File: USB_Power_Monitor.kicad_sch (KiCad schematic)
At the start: 55 parts, among them IC1 MCS1826GQTE-05-P, J1 USB_C_Receptacle, J2 USB_C_Plug, J5 Conn_01x01, J6 Conn_01x01, SW1 SW_Push_Dual, U1 RP2040, U2 L7983PU33R, U3 W25Q16JVSS, U4 TS3USB221AQRSERQ1, Y1 ABM8-272-T3

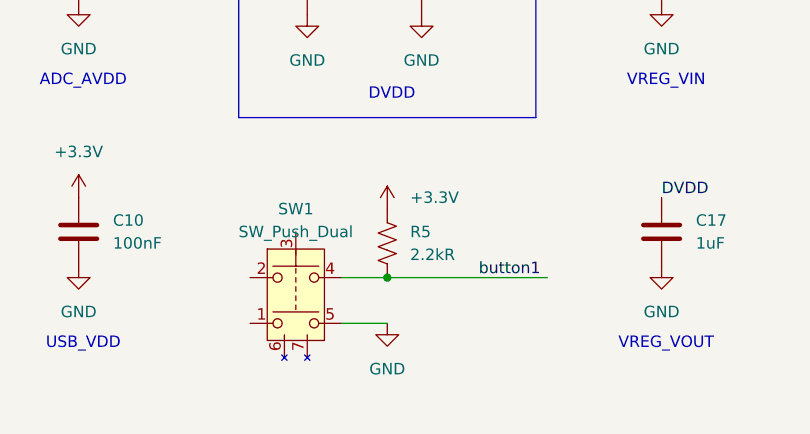
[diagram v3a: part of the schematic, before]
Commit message: All nets routed, need to clean up text and check errors
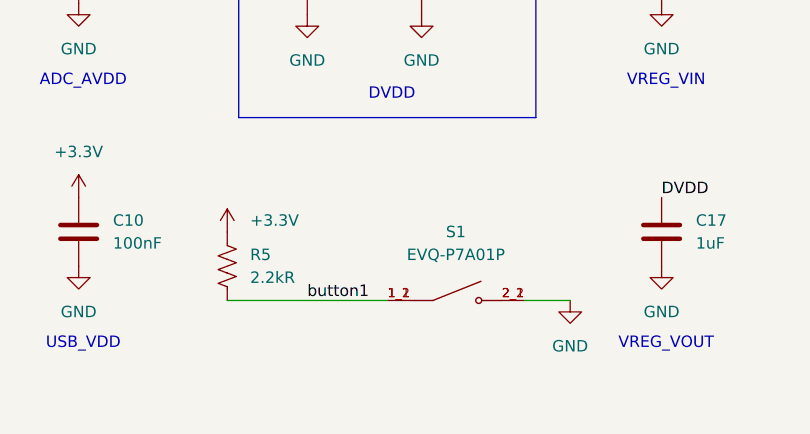
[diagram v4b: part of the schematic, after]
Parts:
- removed SW1: SW_Push_Dual, KMS231GPLFS:SMT_231GPLFS, symbol Switch:SW_Push_Dual
- added S1: EVQ-P7A01P, EVQ-P7A01P:SW_EVQ-P7A01P, symbol EVQ-P7A01P:EVQ-P7A01P
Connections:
- net GND: now also S1.2_1, S1.2_2
- net button1: now also S1.1_1, S1.1_2
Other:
- moved on the sheet: R5
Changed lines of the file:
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@@
 	)
 	(junction
-		(at 59.69 180.34)
-		(diameter 0)
-		(color 0 0 0 0)
-	)
-	(junction
 		(at 224.79 114.3)
 		(diameter 0)
@@
 	(wire
 		(pts
-			(xy 59.69 180.34) (xy 77.47 180.34)
+			(xy 41.91 182.88) (xy 59.69 182.88)
 		)
 		(stroke
@@
 	(wire
 		(pts
-			(xy 54.61 180.34) (xy 59.69 180.34)
-		)
-		(stroke
-			(width 0)
-			(type default)
-		)
-	)
-	(wire
-		(pts
 			(xy 138.43 59.69) (xy 149.86 59.69)
 		)
@@
 	(wire
 		(pts
-			(xy 54.61 185.42) (xy 59.69 185.42)
+			(xy 74.93 182.88) (xy 80.01 182.88)
 		)
 		(stroke
@@
 	)
 	(label "button1"
-		(at 69.85 180.34 0)
+		(at 50.8 182.88 0)
 		(effects
 			(font
@@
 	(symbol
 		(lib_id "power:+3.3V")
-		(at 59.69 172.72 0)
+		(at 41.91 175.26 0)
 		(unit 1)
 		(exclude_from_sim no)
@@
 		(fields_autoplaced yes)
 		(property "Reference" "#PWR052"
-			(at 59.69 176.53 0)
+			(at 41.91 179.07 0)
 			(effects
 				(font
@@
 		)
 		(property "Value" "+3.3V"
-			(at 62.23 171.4499 0)
+			(at 44.45 173.9899 0)
 			(effects
 				(font
@@
 		)
 		(property "Footprint" ""
-			(at 59.69 172.72 0)
+			(at 41.91 175.26 0)
 			(effects
 				(font
@@
 		)
 		(property "Datasheet" ""
-			(at 59.69 172.72 0)
+			(at 41.91 175.26 0)
 			(effects
 				(font
@@
 		)
 		(property "Description" "Power symbol creates a global label with name \"+3.3V\""
-			(at 59.69 172.72 0)
+			(at 41.91 175.26 0)
 			(effects
 				(font
@@
 	)
 	(symbol
-		(lib_id "Switch:SW_Push_Dual")
-		(at 49.53 182.88 0)
-		(unit 1)
-		(exclude_from_sim no)
-		(in_bom yes)
-		(on_board yes)
-		(dnp no)
-		(fields_autoplaced yes)
-		(property "Reference" "SW1"
-			(at 49.53 172.72 0)
-			(effects
-				(font
-					(size 1.27 1.27)
-				)
-			)
-		)
-		(property "Value" "SW_Push_Dual"
-			(at 49.53 175.26 0)
-			(effects
-				(font
-					(size 1.27 1.27)
-				)
-			)
-		)
-		(property "Footprint" "KMS231GPLFS:SMT_231GPLFS"
-			(at 49.53 175.26 0)
-			(effects
-				(font
-					(size 1.27 1.27)
-				)
-				(hide yes)
-			)
-		)
-		(property "Datasheet" "~"
-			(at 49.53 182.88 0)
-			(effects
-				(font
-					(size 1.27 1.27)
-				)
-				(hide yes)
-			)
-		)
-		(property "Description" "Push button switch, generic, symbol, four pins"
-			(at 49.53 182.88 0)
-			(effects
-				(font
-					(size 1.27 1.27)
-				)
-				(hide yes)
-			)
-		)
-		(property "KLC_S4.2_DVDD" ""
-			(at 49.53 182.88 0)
-			(effects
-				(font
-					(size 1.27 1.27)
-				)
-				(hide yes)
-			)
-		)
-		(property "KLC_S4.2_VREG_VOUT" ""
-			(at 49.53 182.88 0)
-			(effects
-				(font
-					(size 1.27 1.27)
-				)
-				(hide yes)
-			)
-		)
-		(property "Manufacturer_Name" "C&K"
-			(at 49.53 182.88 0)
-			(effects
-				(font
-					(size 1.27 1.27)
-				)
-				(hide yes)
-			)
-		)
-		(property "Manufacturer_Part_Number" "KMS231GP LFS"
-			(at 49.53 182.88 0)
-			(effects
-				(font
-					(size 1.27 1.27)
-				)
-				(hide yes)
-			)
-		)
-		(pin "4"
-		)
-		(pin "2"
-		)
-		(pin "3"
-		)
-		(pin "1"
-		)
-		(pin "5"
-		)
-		(pin "7"
-		)
-		(pin "6"
-		)
-		(instances
-			(project ""
-				(path "/e9e64cba-d7b8-4c36-9924-3031f0f5d4f4"
-					(reference "SW1")
-					(unit 1)
-				)
-			)
-		)
-	)
-	(symbol
 		(lib_id "power:GND")
 		(at 73.66 87.63 0)
@@
 	)
 	(symbol
+		(lib_id "EVQ-P7A01P:EVQ-P7A01P")
+		(at 67.31 182.88 0)
+		(unit 1)
+		(exclude_from_sim no)
+		(in_bom yes)
+		(on_board yes)
+		(dnp no)
+		(fields_autoplaced yes)
+		(property "Reference" "S1"
+			(at 67.31 175.26 0)
+			(effects
+				(font
+					(size 1.27 1.27)
+				)
+			)
+		)
+		(property "Value" "EVQ-P7A01P"
+			(at 67.31 177.8 0)
+			(effects
+				(font
+					(size 1.27 1.27)
+				)
+			)
+		)
+		(property "Footprint" "EVQ-P7A01P:SW_EVQ-P7A01P"
+			(at 67.31 182.88 0)
+			(effects
+				(font
+					(size 1.27 1.27)
+				)
+				(justify bottom)
+				(hide yes)
+			)
+		)
+		(property "Datasheet" ""
+			(at 67.31 182.88 0)
+			(effects
+				(font
+					(size 1.27 1.27)
+				)
+				(hide yes)
+			)
+		)
+		(property "Description" ""
+			(at 67.31 182.88 0)
+			(effects
+				(font
+					(size 1.27 1.27)
+				)
+				(hide yes)
+			)
+		)
+		(property "PARTREV" "2022.4"
+			(at 67.31 182.88 0)
+			(effects
+				(font
+					(size 1.27 1.27)
+				)
+				(justify bottom)
+				(hide yes)
+			)
+		)
+		(property "STANDARD" "Manufacturer Recommendations"
+			(at 67.31 182.88 0)
+			(effects
+				(font
+					(size 1.27 1.27)
+				)
+				(justify bottom)
+				(hide yes)
+			)
+		)
+		(property "MAXIMUM_PACKAGE_HEIGHT" "1.35mm"
+			(at 67.31 182.88 0)
+			(effects
+				(font
+					(size 1.27 1.27)
+				)
+				(justify bottom)
+				(hide yes)
+			)
+		)
+		(property "MANUFACTURER" "Panasonic Electronic Components"
+			(at 67.31 182.88 0)
+			(effects
+				(font
+					(size 1.27 1.27)
+				)
+				(justify bottom)
+				(hide yes)
+			)
+		)
+		(pin "1_2"
+		)
+		(pin "2_1"
+		)
+		(pin "1_1"
+		)
+		(pin "2_2"
+		)
+		(instances
+			(project ""
+				(path "/e9e64cba-d7b8-4c36-9924-3031f0f5d4f4"
+					(reference "S1")
+					(unit 1)
+				)
+			)
+		)
+	)
+	(symbol
 		(lib_id "Connector:TestPoint")
 		(at 120.65 119.38 90)
@@
 	(symbol
 		(lib_id "Device:R_US")
-		(at 59.69 176.53 0)
+		(at 41.91 179.07 0)
 		(unit 1)
 		(exclude_from_sim no)
@@
 		(fields_autoplaced yes)
 		(property "Reference" "R5"
-			(at 62.23 175.2599 0)
+			(at 44.45 177.7999 0)
 			(effects
 				(font
@@
 		)
 		(property "Value" "2.2kR"
-			(at 62.23 177.7999 0)
+			(at 44.45 180.3399 0)
 			(effects
 				(font
@@
 		)
 		(property "Footprint" "Capacitor_SMD:C_0603_1608Metric"
-			(at 60.706 176.784 90)
+			(at 42.926 179.324 90)
 			(effects
 				(font
@@
 		)
 		(property "Datasheet" "~"
-			(at 59.69 176.53 0)
+			(at 41.91 179.07 0)
 			(effects
 				(font
@@
 		)
 		(property "Description" "Resistor, US symbol"
-			(at 59.69 176.53 0)
+			(at 41.91 179.07 0)
 			(effects
 				(font
@@
 		)
 		(property "KLC_S4.2_DVDD" ""
-			(at 59.69 176.53 0)
+			(at 41.91 179.07 0)
 			(effects
 				(font
@@
 		)
 		(property "KLC_S4.2_VREG_VOUT" ""
-			(at 59.69 176.53 0)
+			(at 41.91 179.07 0)
 			(effects
 				(font
@@
 		)
 		(property "Manufacturer_Name" "YAGEO"
-			(at 59.69 176.53 0)
+			(at 41.91 179.07 0)
 			(effects
 				(font
@@
 		)
 		(property "Manufacturer_Part_Number" "RC0603FR-072K2L"
-			(at 59.69 176.53 0)
+			(at 41.91 179.07 0)
 			(effects
 				(font
@@
 	(symbol
 		(lib_id "power:GND")
-		(at 59.69 185.42 0)
+		(at 80.01 182.88 0)
 		(unit 1)
 		(exclude_from_sim no)
@@
 		(fields_autoplaced yes)
 		(property "Reference" "#PWR03"
-			(at 59.69 191.77 0)
+			(at 80.01 189.23 0)
 			(effects
 				(font
@@
 		)
 		(property "Value" "GND"
-			(at 59.69 190.5 0)
+			(at 80.01 187.96 0)
 			(effects
 				(font
@@
 		)
 		(property "Footprint" ""
-			(at 59.69 185.42 0)
+			(at 80.01 182.88 0)
 			(effects
 				(font
@@
 		)
 		(property "Datasheet" ""
-			(at 59.69 185.42 0)
+			(at 80.01 182.88 0)
 			(effects
 				(font
@@
 		)
 		(property "Description" "Power symbol creates a global label with name \"GND\" , ground"
-			(at 59.69 185.42 0)
+			(at 80.01 182.88 0)
 			(effects
 				(font

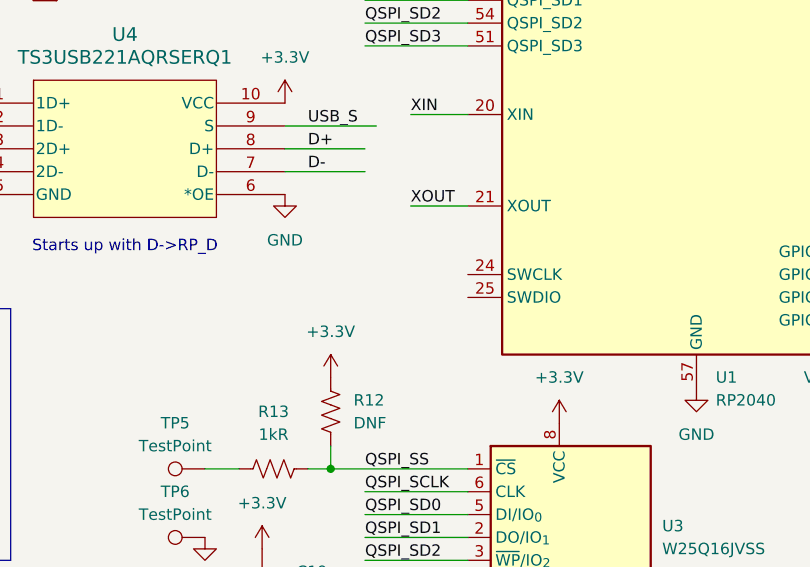
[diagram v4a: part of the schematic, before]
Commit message: Added SWD test points, roughly length matched qspi
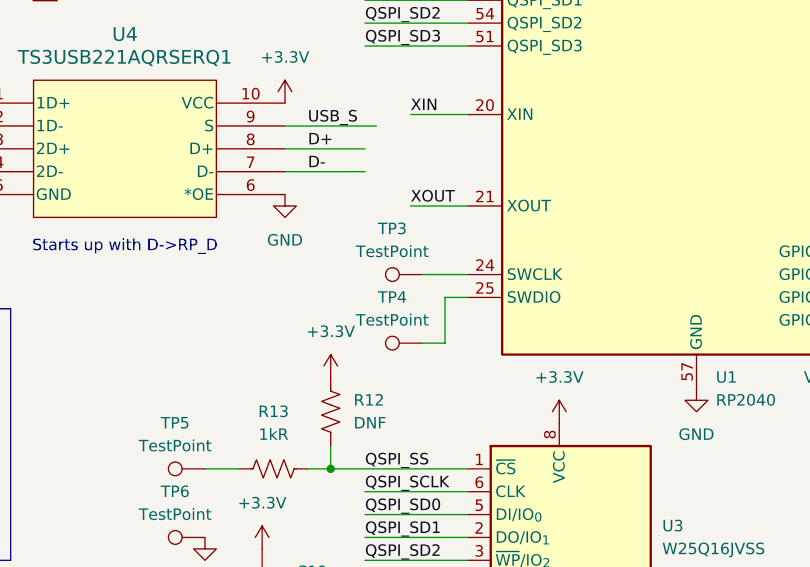
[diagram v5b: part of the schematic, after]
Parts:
- added TP3, TP4: TestPoint, TestPoint:TestPoint_Pad_1.0x1.0mm, symbol Connector:TestPoint
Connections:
- net at U1.24 (SWCLK): now also TP3.1
- net at U1.25 (SWDIO): now also TP4.1

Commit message: Fix BOM part numbers
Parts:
- J5, J6: now left out of the parts list
- R4: Manufacturer_Part_Number RC0805FR-07499RL -> RC0603FR-07499RL
- S1: Manufacturer_Name (none) -> Panasonic Electronic Components; Manufacturer_Part_Number (none) -> EVQ-P7A01P
- U3: Manufacturer_Name (none) -> Winbond Electronics; Manufacturer_Part_Number (none) -> W25Q16JVSSIQ TR
- U4: Manufacturer_Name (none) -> Texas Instruments; Manufacturer_Part_Number (none) -> TS3USB221AQRSERQ1
- Y1: Manufacturer_Name (none) -> Abracon LLC; Manufacturer_Part_Number (none) -> ABM8-272-T3
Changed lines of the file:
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@@
 		(unit 1)
 		(exclude_from_sim no)
-		(in_bom yes)
+		(in_bom no)
 		(on_board yes)
 		(dnp no)
@@
 			)
 		)
+		(property "Manufacturer_Name" "Panasonic Electronic Components"
+			(at 67.31 182.88 0)
+			(effects
+				(font
+					(size 1.27 1.27)
+				)
+				(hide yes)
+			)
+		)
+		(property "Manufacturer_Part_Number" "EVQ-P7A01P"
+			(at 67.31 182.88 0)
+			(effects
+				(font
+					(size 1.27 1.27)
+				)
+				(hide yes)
+			)
+		)
 		(pin "1_2"
 		)
@@
 			)
 		)
+		(property "Manufacturer_Name" "Texas Instruments"
+			(at 93.98 78.74 0)
+			(effects
+				(font
+					(size 1.27 1.27)
+				)
+				(hide yes)
+			)
+		)
+		(property "Manufacturer_Part_Number" "TS3USB221AQRSERQ1"
+			(at 93.98 78.74 0)
+			(effects
+				(font
+					(size 1.27 1.27)
+				)
+				(hide yes)
+			)
+		)
 		(pin "7"
 		)
@@
 			)
 		)
+		(property "Manufacturer_Name" "Winbond Electronics"
+			(at 160.02 127 0)
+			(effects
+				(font
+					(size 1.27 1.27)
+				)
+				(hide yes)
+			)
+		)
+		(property "Manufacturer_Part_Number" "W25Q16JVSSIQ TR"
+			(at 160.02 127 0)
+			(effects
+				(font
+					(size 1.27 1.27)
+				)
+				(hide yes)
+			)
+		)
 		(pin "4"
 		)
@@
 			)
 		)
+		(property "Manufacturer_Name" "Abracon LLC"
+			(at 215.9 152.4 0)
+			(effects
+				(font
+					(size 1.27 1.27)
+				)
+				(hide yes)
+			)
+		)
+		(property "Manufacturer_Part_Number" "ABM8-272-T3"
+			(at 215.9 152.4 0)
+			(effects
+				(font
+					(size 1.27 1.27)
+				)
+				(hide yes)
+			)
+		)
 		(pin "4"
 		)
@@
 			)
 		)
-		(property "Manufacturer_Part_Number" "RC0805FR-07499RL"
+		(property "Manufacturer_Part_Number" "RC0603FR-07499RL"
 			(at 270.51 123.19 0)
 			(effects
@@
 		(unit 1)
 		(exclude_from_sim no)
-		(in_bom yes)
+		(in_bom no)
 		(on_board yes)
 		(dnp no)

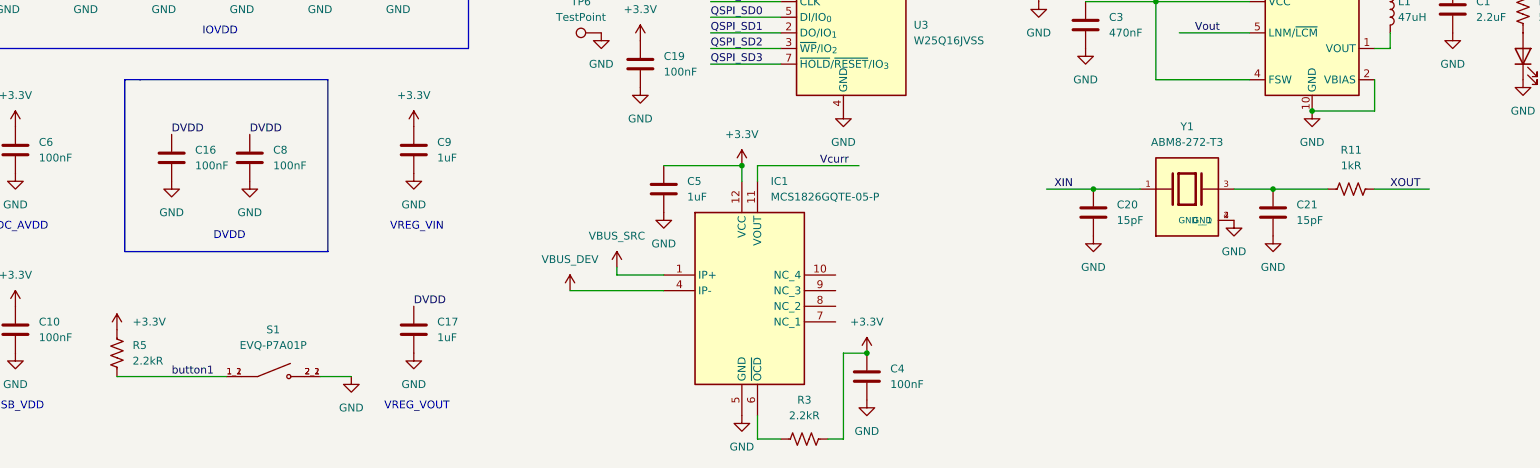
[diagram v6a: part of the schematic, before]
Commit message: Fixed GND plane, add mounting holes
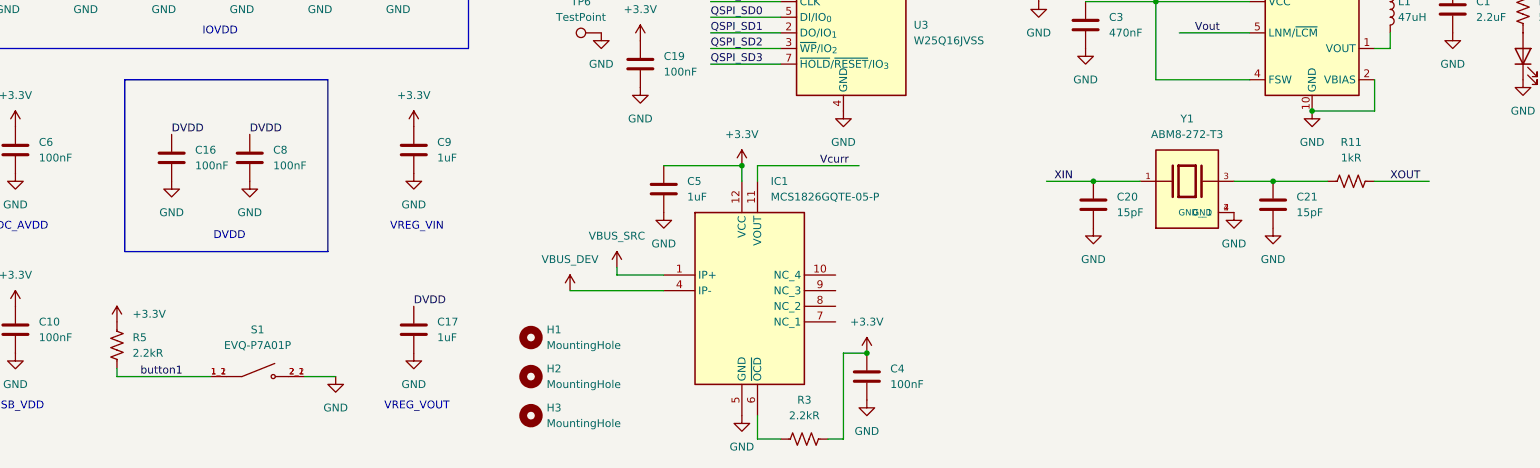
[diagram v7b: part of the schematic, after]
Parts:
- added H1, H2, H3: MountingHole, MountingHole:MountingHole_2.2mm_M2, symbol Mechanical:MountingHole
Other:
- title: (none) -> USB Power Monitor
- moved on the sheet: C20, C21, R11, R5, S1, Y1
